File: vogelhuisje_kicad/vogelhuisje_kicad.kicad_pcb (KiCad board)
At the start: 2 copper layers, 95 x 115 mm, 21 parts, among them J1 Conn_01x02_Female, J2 Conn_01x02, J3 USB_C_Receptacle_USB2.0, J6 Conn_01x19_Female, P1 TP4056breakout, P2 GenericBoostConverter, Q1 Q_PMOS_GSD, U3 ESP32-LilyGo-T_PCIE, U4 PMS5003, U5 SD-card-reader, U6 BME280Breakout, U7 BME280Breakout

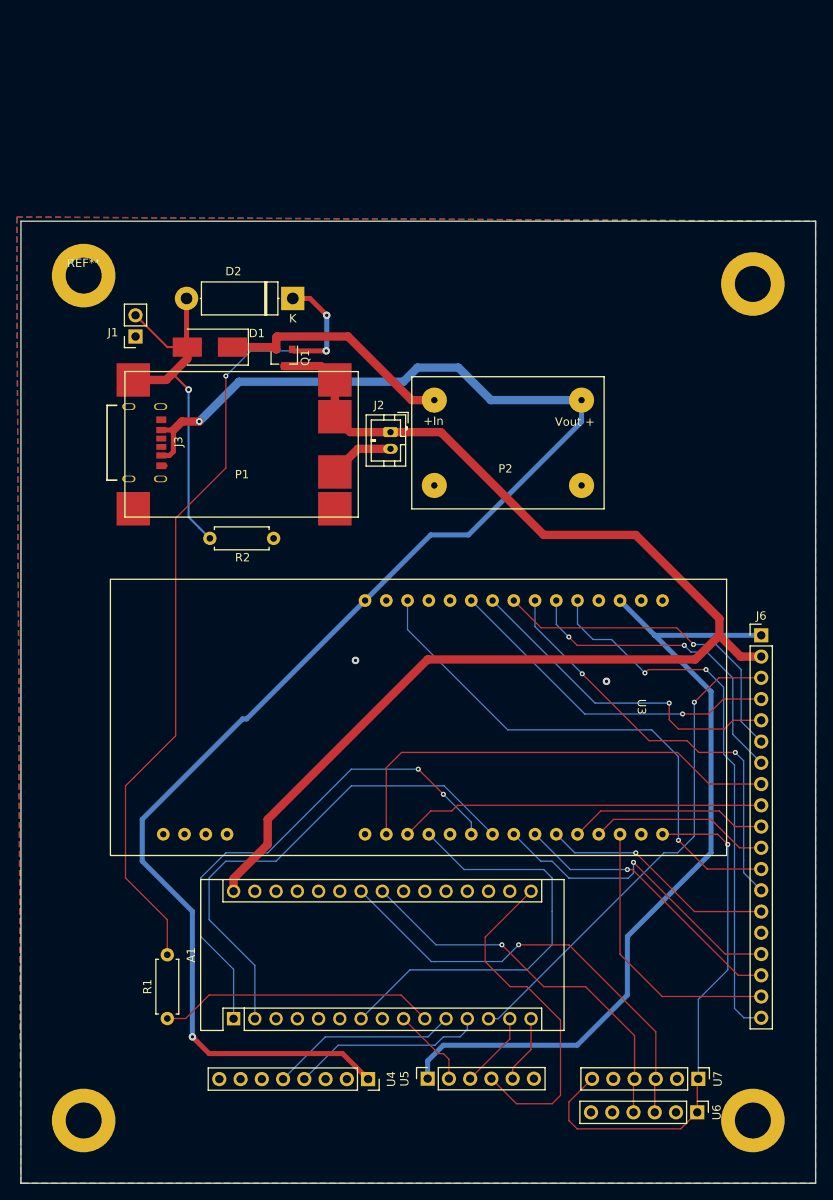
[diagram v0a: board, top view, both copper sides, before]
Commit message: Kicad Changes Tadjiro
Board now supports 3 lipo cells and a motion sensor.
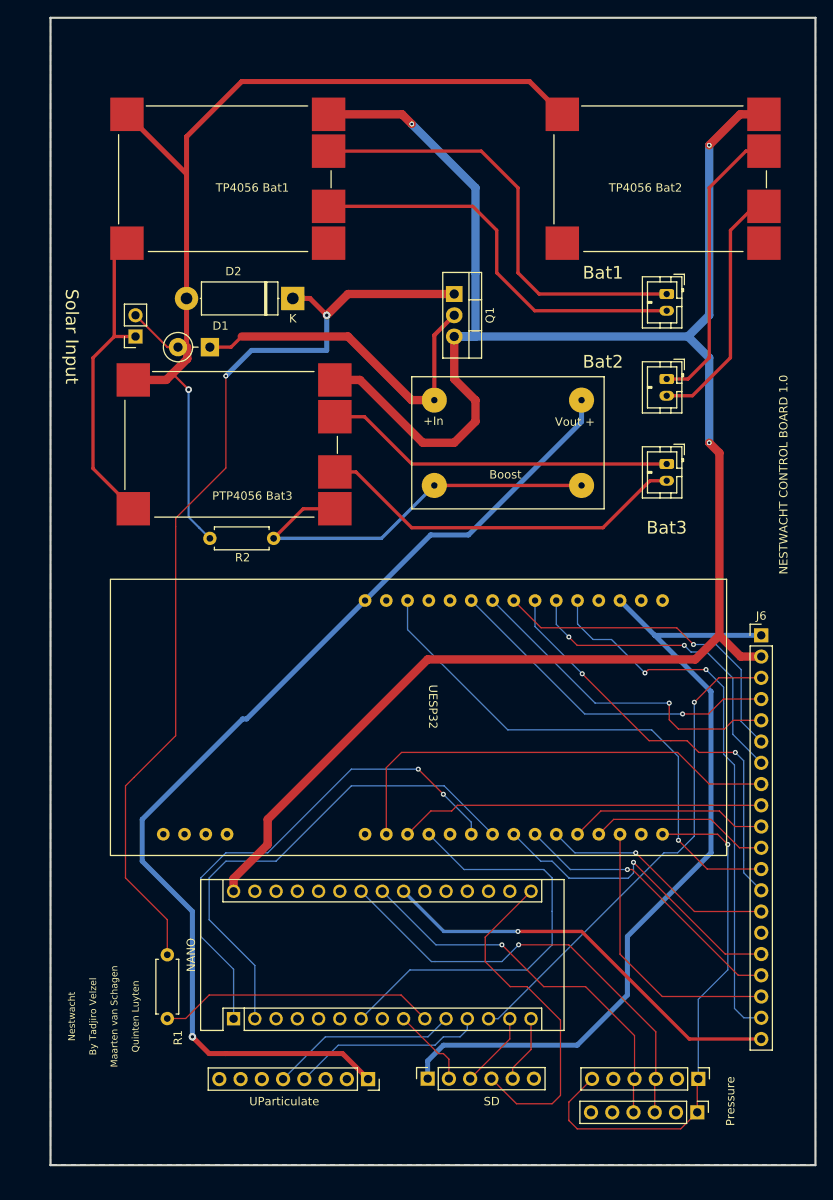
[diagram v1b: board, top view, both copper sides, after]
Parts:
- removed ? (x3): , 
- removed J3: USB_C_Receptacle_USB2.0, components:GCT_USB4125-GF-A-0190_REVA2
- removed REF**: MountingHole_4.3mm_M4_ISO7380_Pad, MountingHole:MountingHole_4.3mm_M4_ISO7380_Pad
- added JBatt1: Batt3, Connector_JST:JST_PH_B2B-PH-K_1x02_P2.00mm_Vertical, F.Cu at (139.7, 86.4)
- added JBattery2: JBatt2, Connector_JST:JST_PH_B2B-PH-K_1x02_P2.00mm_Vertical, F.Cu at (139.7, 76.2)
- added TP4056 Bat1: TP4056breakout, components:TP4056breakout, F.Cu at (74.2, 71.1)
- added TP4056 Bat2: TP4056breakout, components:TP4056breakout, F.Cu at (126.2, 71.1)
- D1: footprint Diode_SMD:D_SMB_Handsoldering -> Diode_THT:D_DO-41_SOD81_P3.81mm_Vertical_KathodeUp
- J6: value Conn_01x19_Female -> Conn_01x20_Female; footprint Connector_PinHeader_2.54mm:PinHeader_1x19_P2.54mm_Vertical -> Connector_PinHeader_2.54mm:PinHeader_1x20_P2.54mm_Vertical
- JBatt3: renamed from J2; value Conn_01x02 -> Batt1
- PTP4056 Bat3: renamed from P1; footprint Components:TP4056breakout -> components:TP4056breakout
- Q1: footprint Package_TO_SOT_SMD:SOT-23 -> Package_TO_SOT_THT:TO-220-3_Vertical
- moved JBatt3 33.2 mm to (139.7, 96.5)
- moved Q1 21.7 mm to (114.3, 76.2)
- renumbered P2 to Boost, J1 to JSolar1, A1 to NANO, U7 to Pressure, U5 to SD, U3 to UESP32, U4 to UParticulate
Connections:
- JBatt3 pad 1: /Power Supply/Vbat -> Net-(JBatt3-Pad1)
- NANO pad 22: unconnected-(A1-Pad22) -> /Sensors and microcontrollers/Motion_out
- PTP4056 Bat3 pad 4: /Power Supply/Vbat -> Net-(JBatt3-Pad1)
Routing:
- net /Power Supply/Vbat: track 148.5 -> 250.4 mm, vias 0 -> 3
- net GND: track 0.73 -> 86.2 mm, vias 2 -> 0
- net Net-(D1-Pad2): track 43.9 -> 122.6 mm
- net +5V: track 185.5 -> 126.4 mm, vias 2 -> 1
- net Net-(JBattery2-Pad1): track 0.00 -> 53.4 mm
- net /Sensors and microcontrollers/Motion_out: track 0.00 -> 50.1 mm, vias 0 -> 1
- net Net-(JBattery2-Pad2): track 0.00 -> 48.6 mm
- net Net-(JBatt3-Pad1): track 0.00 -> 42.0 mm
- net Net-(JBatt3-Pad2): track 7.79 -> 44.8 mm
- net Net-(JBatt1-Pad1): track 0.00 -> 34.8 mm
- net Net-(JBatt1-Pad2): track 0.00 -> 29.9 mm
- net Net-(D1-Pad1): track 28.9 -> 41.6 mm
- net Net-(D2-Pad1): track 102.8 -> 114.9 mm, vias 3 -> 2
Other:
- board size 95 x 115 mm -> 91.4 x 137.2 mm
- board text added: "Bat1"
- board text added: "Bat2"
- board text added: "Bat3"
- board text added: "By Tadjiro Velzel"
- board text added: "Maarten van Schagen"
- board text added: "NESTWACHT CONTROL BOARD 1.0"
- board text added: "Nestwacht"
- board text added: "Quinten Luyten"
- board text added: "Solar Input"

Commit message: Update main board
Ground port added to connector
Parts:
- J6: value Conn_01x20_Female -> Conn_01x21_Female; footprint Connector_PinHeader_2.54mm:PinHeader_1x20_P2.54mm_Vertical -> Connector_PinHeader_2.54mm:PinHeader_1x21_P2.54mm_Vertical
- P3: renamed from TP4056 Bat2
- P4: renamed from TP4056 Bat1
- moved J6 2.73 mm to (151.4, 114.3)
- renumbered NANO to A1, Boost to P2, UESP32 to U3, UParticulate to U4, SD to U5, Pressure to U7
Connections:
- J6 pad 1: +3V3 -> GND
- J6 pad 10: /Sensors and microcontrollers/Y8_CAM -> /Sensors and microcontrollers/Y7_CAM
- J6 pad 11: /Sensors and microcontrollers/Y9_CAM -> /Sensors and microcontrollers/Y8_CAM
- J6 pad 12: /Sensors and microcontrollers/XCLK_CAM -> /Sensors and microcontrollers/Y9_CAM
- J6 pad 13: /Sensors and microcontrollers/HREF_CAM -> /Sensors and microcontrollers/XCLK_CAM
- J6 pad 14: /Sensors and microcontrollers/VSYNC_CAM -> /Sensors and microcontrollers/HREF_CAM
- J6 pad 15: /Sensors and microcontrollers/CAM_RST -> /Sensors and microcontrollers/VSYNC_CAM
- J6 pad 16: /Sensors and microcontrollers/SOIC_CAM -> /Sensors and microcontrollers/CAM_RST
- J6 pad 17: /Sensors and microcontrollers/SIOD_CAM -> /Sensors and microcontrollers/SOIC_CAM
- J6 pad 18: /Sensors and microcontrollers/PWDN_CAM -> /Sensors and microcontrollers/SIOD_CAM
- J6 pad 19: /Sensors and microcontrollers/PCLK_CAM -> /Sensors and microcontrollers/PWDN_CAM
- J6 pad 2: /Power Supply/Vbat -> +3V3
- J6 pad 20: /Sensors and microcontrollers/Motion_out -> /Sensors and microcontrollers/PCLK_CAM
- J6 pad 3: /Sensors and microcontrollers/LED_EN -> /Power Supply/Vbat
- J6 pad 4: /Sensors and microcontrollers/Y2_CAM -> /Sensors and microcontrollers/LED_EN
- J6 pad 5: /Sensors and microcontrollers/Y3_CAM -> /Sensors and microcontrollers/Y2_CAM
- J6 pad 6: /Sensors and microcontrollers/Y4_CAM -> /Sensors and microcontrollers/Y3_CAM
- J6 pad 7: /Sensors and microcontrollers/Y5_CAM -> /Sensors and microcontrollers/Y4_CAM
- J6 pad 8: /Sensors and microcontrollers/Y6_CAM -> /Sensors and microcontrollers/Y5_CAM
- J6 pad 9: /Sensors and microcontrollers/Y7_CAM -> /Sensors and microcontrollers/Y6_CAM
